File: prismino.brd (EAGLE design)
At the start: 50 x 50 mm, 32 parts, among them IC1 NCP1117DT05BDTRKG, J1 ISP-6PIN, Q1 16MHz, U1 ATMEGA32U4

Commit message: Updated everything
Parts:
- removed R6: 1K, rcl:R0805
- BTN1: device karl_new:BUTTON -> robopoly:BUTTON
- C5: value 10uF -> 100nF
- C6: value 100nF -> 10uF
- EXTPOWER: device karl_new:4UCON-18741 -> robopoly:4UCON-18741
- JP1: device karl_new:USB-MICROB-4UCON -> robopoly:USB-MICROB-4UCON
- R2: value 10K -> 1K
- R5: value 1K -> 10K
- moved R2 35.0 mm to (4.50, 39.5), turned to 90 degrees
- moved R5 33.7 mm to (38.0, 29.5), turned to 0 degrees
- moved R1 23.9 mm to (4.50, 33.0), turned to 90 degrees
- moved C5 23.1 mm to (2.00, 46.0)
- moved C6 23.1 mm to (9.00, 24.0)
- moved R3 4.00 mm to (38.0, 17.5)
- moved R4 4.00 mm to (38.0, 21.5)
- renumbered LED1 to LED, LED2 to PWR
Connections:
- net AREF: now also C5.1; no longer C6.1
- net BOOTEN: no longer R1.2
- net D13: now also R2.2; no longer R6.2
- net DM: now also R3.1; no longer R4.1
- net DP: now also R4.1; no longer R3.1
- net GND: no longer R1.1
- net N$11: now also R2.1; no longer R6.1
- net N$3: now also R1.1; no longer R5.1
- net N$6: now also R3.2; no longer R4.2
- net N$7: now also R4.2; no longer R3.2
- net RESET: now also R5.1; no longer BTN1.4, R2.1
- net VCC: now also C6.1, R1.2; no longer C5.1, R2.2
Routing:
- net RESET: track 92.3 -> 83.2 mm
- net BOOTEN: track 6.33 -> 3.02 mm
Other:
- outline, holes or cut-outs redrawn
- board text added: "16 MHz"
- board text added: "Kangur - 2014"
- board text added: "Ver. 2"
- board text removed: "16MHz"
- board text removed: "Kangur - 2013"
- board text removed: "R6"
- board text removed: "Ver. 1"

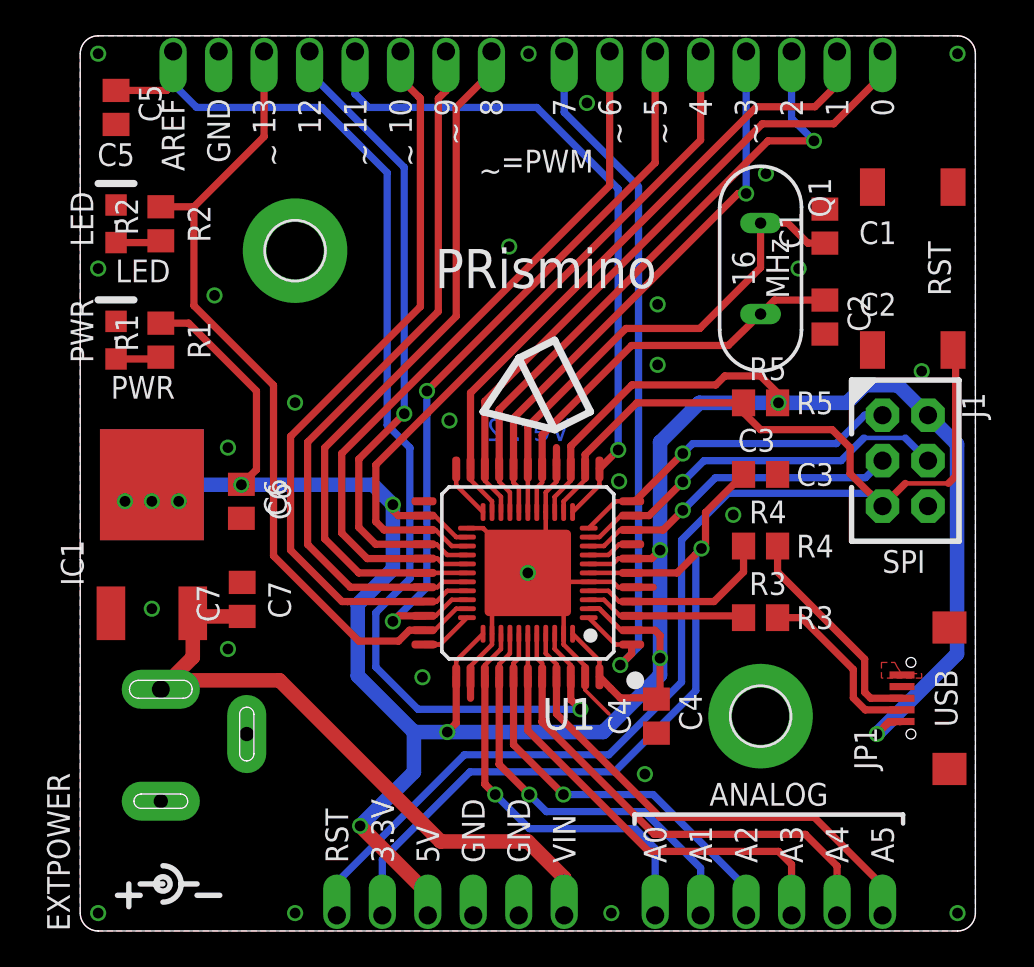
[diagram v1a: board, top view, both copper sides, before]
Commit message: Tested
The board was soldered, tested and proven to work. Some silkscreen
markings were corrected for aesthetics.
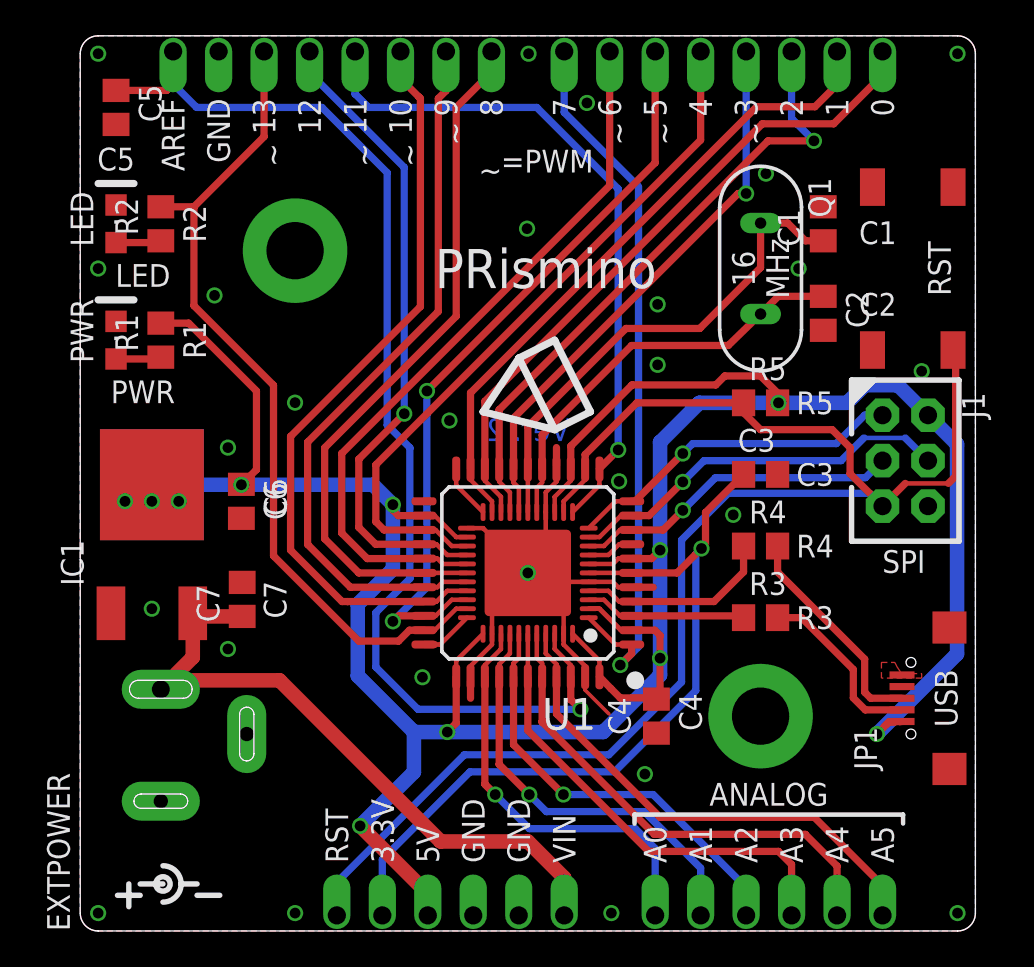
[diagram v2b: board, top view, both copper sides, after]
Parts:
- J1: device robopoly:2X3-NOSILK -> robopoly:2X3-NOSILK-STACK
- moved C2 0.23 mm to (41.5, 34.5)
- moved C1 0.16 mm to (41.5, 39.5)
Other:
- board text added: "2014-03-04"
- board text added: "Licence: CC-BY-SA"
- board text added: "Version: 2"
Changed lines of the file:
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@@
 <layer number="21" name="tPlace" color="7" fill="1" visible="yes" active="yes"/>
 <layer number="22" name="bPlace" color="7" fill="1" visible="yes" active="yes"/>
-<layer number="23" name="tOrigins" color="15" fill="1" visible="no" active="yes"/>
-<layer number="24" name="bOrigins" color="15" fill="1" visible="no" active="yes"/>
+<layer number="23" name="tOrigins" color="15" fill="1" visible="yes" active="yes"/>
+<layer number="24" name="bOrigins" color="15" fill="1" visible="yes" active="yes"/>
 <layer number="25" name="tNames" color="7" fill="1" visible="no" active="yes"/>
 <layer number="26" name="bNames" color="7" fill="1" visible="no" active="yes"/>
@@
 <layer number="220" name="220bmp" color="21" fill="1" visible="no" active="no"/>
 <layer number="221" name="221bmp" color="22" fill="1" visible="no" active="no"/>
-<layer number="222" name="222bmp" color="23" fill="1" visible="no" active="no"/>
 <layer number="223" name="223bmp" color="24" fill="1" visible="no" active="no"/>
 <layer number="224" name="224bmp" color="25" fill="1" visible="no" active="no"/>
@@
 <text x="15.812" y="44" size="1.27" layer="21" font="vector" ratio="12" rot="R270" align="center-left">~</text>
 <text x="10.732" y="44" size="1.27" layer="21" font="vector" ratio="12" rot="R270" align="center-left">~</text>
-<text x="3.5" y="37.5" size="1.27" layer="21" font="vector" ratio="12" align="top-center">LED</text>
-<text x="3.5" y="31" size="1.27" layer="21" font="vector" ratio="12" align="top-center">PWR</text>
+<text x="3.5" y="37.25" size="1.27" layer="21" font="vector" ratio="12" align="top-center">LED</text>
+<text x="3.5" y="30.75" size="1.27" layer="21" font="vector" ratio="12" align="top-center">PWR</text>
 <text x="30.75" y="12" size="1.27" layer="21" font="vector" ratio="12" rot="R90" align="bottom-center">C4</text>
 <text x="49" y="13" size="1.27" layer="21" font="vector" ratio="12" rot="R90" align="bottom-center">USB</text>
@@
 <text x="40" y="21.5" size="1.27" layer="21" font="vector" ratio="12" align="center-left">R4</text>
 <text x="40" y="17.5" size="1.27" layer="21" font="vector" ratio="12" align="center-left">R3</text>
-<text x="10.5" y="24" size="1.27" layer="21" font="vector" ratio="12" rot="R90" align="top-center">C6</text>
-<text x="10.5" y="18.5" size="1.27" layer="21" font="vector" ratio="12" rot="R90" align="top-center">C7</text>
-<text x="6" y="39.5" size="1.27" layer="21" font="vector" ratio="12" rot="R90" align="top-center">R2</text>
-<text x="6" y="33" size="1.27" layer="21" font="vector" ratio="12" rot="R90" align="top-center">R1</text>
+<text x="10.25" y="24" size="1.27" layer="21" font="vector" ratio="12" rot="R90" align="top-center">C6</text>
+<text x="10.25" y="18.5" size="1.27" layer="21" font="vector" ratio="12" rot="R90" align="top-center">C7</text>
+<text x="5.75" y="39.5" size="1.27" layer="21" font="vector" ratio="12" rot="R90" align="top-center">R2</text>
+<text x="5.75" y="33" size="1.27" layer="21" font="vector" ratio="12" rot="R90" align="top-center">R1</text>
 <wire x1="1" y1="35.25" x2="3" y2="35.25" width="0.4064" layer="21"/>
 <wire x1="1" y1="41.75" x2="3" y2="41.75" width="0.4064" layer="21"/>
@@
 <text x="17.888" y="46.2" size="1.27" layer="22" font="vector" ratio="12" rot="MR270" align="center-left">A10</text>
 <text x="12.808" y="46.2" size="1.27" layer="22" font="vector" ratio="12" rot="MR270" align="center-left">A11</text>
-<text x="2" y="44" size="1.27" layer="21" font="vector" ratio="12" align="top-center">C5</text>
+<text x="2" y="43.75" size="1.27" layer="21" font="vector" ratio="12" align="top-center">C5</text>
 <text x="48.625" y="37" size="1.27" layer="21" font="vector" ratio="12" rot="R90" align="bottom-center">RST</text>
 <wire x1="43.082" y1="27.77" x2="43.082" y2="30.77" width="0.3048" layer="21"/>
@@
 <vertex x="44.382" y="30.77"/>
 </polygon>
+<text x="0" y="-3" size="1.778" layer="48" font="vector" ratio="12">PRismino</text>
+<text x="50" y="-3" size="1.778" layer="48" font="vector" ratio="12" align="bottom-right">Version: 2</text>
+<text x="50" y="-6" size="1.27" layer="48" font="vector" ratio="12" align="bottom-right">2014-03-04</text>
+<text x="0" y="-6" size="1.27" layer="48" font="vector" ratio="12">http://robopoly.epfl.ch</text>
+<text x="0" y="-9" size="1.27" layer="48" font="vector" ratio="12">Licence: CC-BY-SA</text>
 </plain>
 <attributes>
@@
 <element name="LED" library="led" package="CHIPLED_0805" value="" x="2" y="39.5"/>
 <element name="JP1" library="robopoly" package="USB-MICROB-4UCON" value="USB4UCON" x="50" y="13" rot="R90"/>
-<element name="J1" library="robopoly" package="2X3-NOSILK" value="ISP-6PIN" x="46.082" y="26.27" rot="R270"/>
+<element name="J1" library="robopoly" package="2X3-NOSILK-STACK" value="ISP-6PIN" x="46.082" y="26.27" rot="R270"/>
 <element name="EXTPOWER" library="robopoly" package="4UCON-18741" value="4UCON-18741" x="4.5" y="0" rot="R90"/>
 <element name="H1" library="robopoly" package="3,2-PAD" value="MOUNT-PAD-ROUND3.2" x="38" y="12"/>
@@
 <element name="BTN1" library="robopoly" package="BUTTON" value="BUTTON" x="46.5" y="37" rot="R180"/>
 <element name="U1" library="robopoly" package="TQFP-44" value="ATMEGA32U4" x="25" y="20" rot="R180"/>
-<element name="C1" library="rcl" package="C0805" value="22pF" x="41.5925" y="39.37" rot="R90"/>
-<element name="C2" library="rcl" package="C0805" value="22pF" x="41.5925" y="34.29" rot="R270"/>
+<element name="C1" library="rcl" package="C0805" value="22pF" x="41.5" y="39.5" rot="R90"/>
+<element name="C2" library="rcl" package="C0805" value="22pF" x="41.5" y="34.5" rot="R270"/>
 <element name="U$4" library="robopoly" package="ROBOPOLY-LOGO-BOTTOM-BIG" value="ROBOPOLY-LOGOBOTTOM-BIG" x="25" y="31.75"/>
 <element name="U$5" library="robopoly" package="OPEN-HARDWARE-BOTTOM-SMALL" value="OPEN-HARDWARE-LOGOBOTTOM-SMALL" x="46" y="34"/>
@@
 <via x="32.25" y="35" extent="1-16" drill="0.6" shape="octagon"/>
 <via x="19.1125" y="14.1725" extent="1-16" drill="0.6" shape="octagon"/>
-<via x="23.9575" y="38.2275" extent="1-16" drill="0.6" shape="octagon"/>
+<via x="24.9575" y="39.2275" extent="1-16" drill="0.6" shape="octagon"/>
 <via x="36.4725" y="23.2425" extent="1-16" drill="0.6" shape="octagon"/>
 <via x="1" y="37" extent="1-16" drill="0.6" shape="octagon"/>
@@
 <wire x1="38" y1="37.0475" x2="38" y2="39.54" width="0.4064" layer="1"/>
 <wire x1="38" y1="39.54" x2="39.5175" y2="39.54" width="0.4064" layer="1"/>
-<wire x1="39.5175" y1="39.54" x2="40.6375" y2="38.42" width="0.4064" layer="1"/>
-<wire x1="40.6375" y1="38.42" x2="41.5925" y2="38.42" width="0.4064" layer="1"/>
+<wire x1="39.5175" y1="39.54" x2="40.5075" y2="38.55" width="0.4064" layer="1"/>
+<wire x1="40.5075" y1="38.55" x2="41.5" y2="38.55" width="0.4064" layer="1"/>
 </signal>
 <signal name="XTAL2">
@@
 <wire x1="36.195" y1="32.7025" x2="38" y2="34.46" width="0.4064" layer="1"/>
 <contactref element="C2" pad="1"/>
-<wire x1="38" y1="34.46" x2="38.78" y2="35.24" width="0.4064" layer="1"/>
-<wire x1="38.78" y1="35.24" x2="41.5925" y2="35.24" width="0.4064" layer="1"/>
 <contactref element="U1" pad="60"/>
 <wire x1="25.5" y1="23.4" x2="25.5" y2="24.75" width="0.254" layer="1"/>
@@
 <wire x1="25.8" y1="25.8" x2="25.8" y2="27.705" width="0.4064" layer="1"/>
 <wire x1="25.8" y1="27.705" x2="30.7975" y2="32.7025" width="0.4064" layer="1"/>
+<wire x1="38" y1="34.46" x2="38.99" y2="35.45" width="0.4064" layer="1"/>
+<wire x1="38.99" y1="35.45" x2="41.5" y2="35.45" width="0.4064" layer="1"/>
 </signal>
 <signal name="DM">
